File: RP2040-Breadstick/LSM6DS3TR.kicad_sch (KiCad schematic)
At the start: 1 part

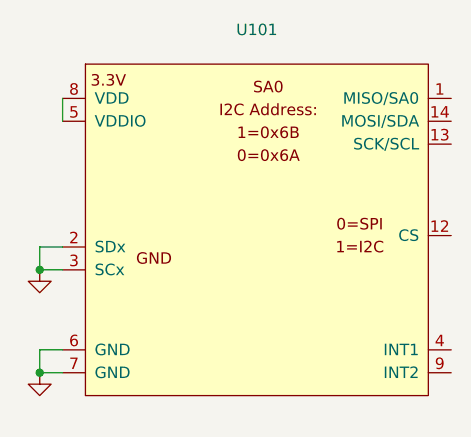
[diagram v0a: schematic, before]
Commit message: Moved Label R108
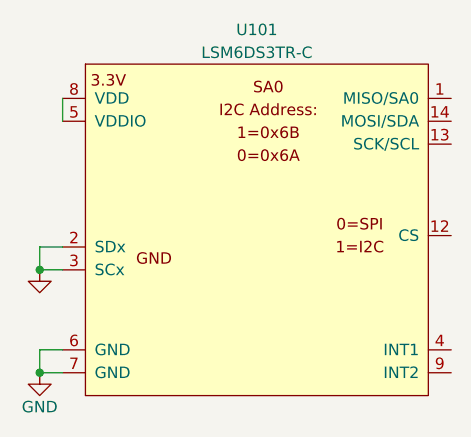
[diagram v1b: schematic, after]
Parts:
- U101: value (none) -> LSM6DS3TR-C; footprint (none) -> LSM6DS3TR-C:LGA-14-2.5X3MM
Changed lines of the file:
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@@
       (effects (font (size 1.27 1.27)) hide)
     )
-    (property "Value" "" (id 1) (at 115.57 102.87 0))
+    (property "Value" "GND" (id 1) (at 115.57 102.87 0))
     (property "Footprint" "" (id 2) (at 115.57 99.06 0)
       (effects (font (size 1.27 1.27)) hide)
@@
     (in_bom yes) (on_board yes) (fields_autoplaced)
     (property "Reference" "U101" (id 0) (at 139.7 60.96 0))
-    (property "Value" "" (id 1) (at 139.7 63.5 0))
-    (property "Footprint" "" (id 2) (at 125.73 104.14 0)
+    (property "Value" "LSM6DS3TR-C" (id 1) (at 139.7 63.5 0))
+    (property "Footprint" "LSM6DS3TR-C:LGA-14-2.5X3MM" (id 2) (at 125.73 104.14 0)
       (effects (font (size 1.27 1.27)) (justify left bottom) hide)
     )

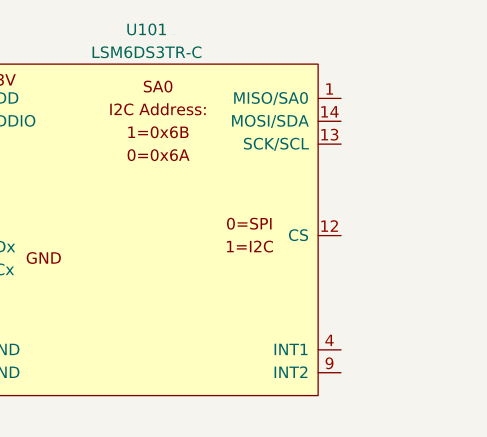
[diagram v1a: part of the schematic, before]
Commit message: IMU Pins and Power Supply updated
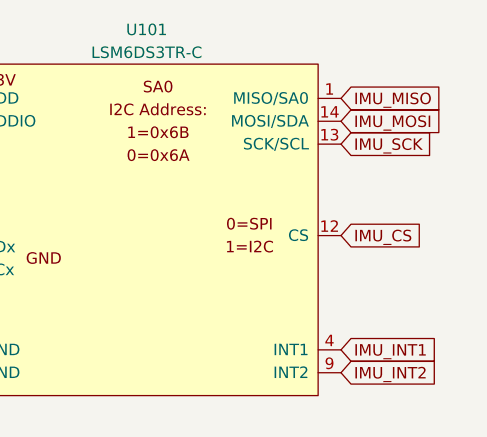
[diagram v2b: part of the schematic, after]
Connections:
- net IMU_MISO: now reaches U101.1 (MISO/SA0)
- net IMU_CS: now reaches U101.12 (CS)
- net IMU_SCK: now reaches U101.13 (SCK/SCL)
- net IMU_MOSI: now reaches U101.14 (MOSI/SDA)
- net IMU_INT1: now reaches U101.4 (INT1)
- net IMU_INT2: now reaches U101.9 (INT2)
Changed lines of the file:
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@@
     (stroke (width 0) (type default) (color 0 0 0 0))
+  )
+  (global_label "IMU_MISO" (shape input) (at 161.29 68.58 0) (fields_autoplaced)
+    (effects (font (size 1.27 1.27)) (justify left))
+    (property "Intersheet References" "${INTERSHEET_REFS}" (id 0) (at 172.6536 68.5006 0)
+      (effects (font (size 1.27 1.27)) (justify left) hide)
+    )
+  )
+  (global_label "IMU_INT1" (shape input) (at 161.29 96.52 0) (fields_autoplaced)
+    (effects (font (size 1.27 1.27)) (justify left))
+    (property "Intersheet References" "${INTERSHEET_REFS}" (id 0) (at 172.1698 96.4406 0)
+      (effects (font (size 1.27 1.27)) (justify left) hide)
+    )
+  )
+  (global_label "IMU_INT2" (shape input) (at 161.29 99.06 0) (fields_autoplaced)
+    (effects (font (size 1.27 1.27)) (justify left))
+    (property "Intersheet References" "${INTERSHEET_REFS}" (id 0) (at 172.1698 98.9806 0)
+      (effects (font (size 1.27 1.27)) (justify left) hide)
+    )
+  )
+  (global_label "IMU_CS" (shape input) (at 161.29 83.82 0) (fields_autoplaced)
+    (effects (font (size 1.27 1.27)) (justify left))
+    (property "Intersheet References" "${INTERSHEET_REFS}" (id 0) (at 170.5369 83.7406 0)
+      (effects (font (size 1.27 1.27)) (justify left) hide)
+    )
+  )
+  (global_label "IMU_SCK" (shape input) (at 161.29 73.66 0) (fields_autoplaced)
+    (effects (font (size 1.27 1.27)) (justify left))
+    (property "Intersheet References" "${INTERSHEET_REFS}" (id 0) (at 171.8069 73.5806 0)
+      (effects (font (size 1.27 1.27)) (justify left) hide)
+    )
+  )
+  (global_label "IMU_MOSI" (shape input) (at 161.29 71.12 0) (fields_autoplaced)
+    (effects (font (size 1.27 1.27)) (justify left))
+    (property "Intersheet References" "${INTERSHEET_REFS}" (id 0) (at 172.6536 71.0406 0)
+      (effects (font (size 1.27 1.27)) (justify left) hide)
+    )
   )
   (symbol (lib_id "power:GND") (at 115.57 99.06 0) (unit 1)

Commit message: Schematic Rough Draft Complete
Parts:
- added C401: 1uF, Breadstick Footprints:Perfect_0201_Cap, symbol Device:C
- renumbered U101 to U401
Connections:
- net GND: now also C401.2
- net 3V3_LDO: now reaches U401.5 (VDDIO), U401.8 (VDD)
- net 3V3_LDO: now also C401.1
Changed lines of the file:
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@@
   (junction (at 115.57 99.06) (diameter 0) (color 0 0 0 0)
+  )
+  (junction (at 118.11 68.58) (diameter 0) (color 0 0 0 0)
+  )
+  (junction (at 105.41 68.58) (diameter 0) (color 0 0 0 0)
   )
   (wire (pts (xy 115.57 85.09) (xy 115.57 87.63))
@@
     (stroke (width 0) (type default) (color 0 0 0 0))
   )
+  (wire (pts (xy 105.41 68.58) (xy 118.11 68.58))
+    (stroke (width 0) (type default) (color 0 0 0 0))
+  )
   (wire (pts (xy 115.57 96.52) (xy 115.57 99.06))
     (stroke (width 0) (type default) (color 0 0 0 0))
@@
   )
   (wire (pts (xy 118.11 85.09) (xy 115.57 85.09))
+    (stroke (width 0) (type default) (color 0 0 0 0))
+  )
+  (wire (pts (xy 105.41 66.04) (xy 105.41 68.58))
     (stroke (width 0) (type default) (color 0 0 0 0))
   )
@@
     )
   )
+  (global_label "3V3_LDO" (shape input) (at 105.41 66.04 180) (fields_autoplaced)
+    (effects (font (size 1.27 1.27)) (justify right))
+    (property "Intersheet References" "${INTERSHEET_REFS}" (id 0) (at 94.8931 66.1194 0)
+      (effects (font (size 1.27 1.27)) (justify right) hide)
+    )
+  )
   (global_label "IMU_MOSI" (shape input) (at 161.29 71.12 0) (fields_autoplaced)
     (effects (font (size 1.27 1.27)) (justify left))
@@
   (symbol (lib_id "power:GND") (at 115.57 99.06 0) (unit 1)
     (in_bom yes) (on_board yes)
-    (property "Reference" "#PWR0107" (id 0) (at 115.57 105.41 0)
+    (property "Reference" "#PWR0403" (id 0) (at 115.57 105.41 0)
       (effects (font (size 1.27 1.27)) hide)
     )
@@
   (symbol (lib_id "LSM6DS3TR-C:LSM6DS3TR-C") (at 139.7 83.82 0) (unit 1)
     (in_bom yes) (on_board yes) (fields_autoplaced)
-    (property "Reference" "U101" (id 0) (at 139.7 60.96 0))
+    (property "Reference" "U401" (id 0) (at 139.7 60.96 0))
     (property "Value" "LSM6DS3TR-C" (id 1) (at 139.7 63.5 0))
     (property "Footprint" "LSM6DS3TR-C:LGA-14-2.5X3MM" (id 2) (at 125.73 104.14 0)
@@
   (symbol (lib_id "power:GND") (at 115.57 87.63 0) (unit 1)
     (in_bom yes) (on_board yes)
-    (property "Reference" "#PWR0106" (id 0) (at 115.57 93.98 0)
+    (property "Reference" "#PWR0402" (id 0) (at 115.57 93.98 0)
       (effects (font (size 1.27 1.27)) hide)
     )
@@
     (pin "1")
   )
+  (symbol (lib_id "power:GND") (at 105.41 76.2 0) (unit 1)
+    (in_bom yes) (on_board yes)
+    (property "Reference" "#PWR0401" (id 0) (at 105.41 82.55 0)
+      (effects (font (size 1.27 1.27)) hide)
+    )
+    (property "Value" "~" (id 1) (at 105.41 80.01 0))
+    (property "Footprint" "" (id 2) (at 105.41 76.2 0)
+      (effects (font (size 1.27 1.27)) hide)
+    )
+    (property "Datasheet" "" (id 3) (at 105.41 76.2 0)
+      (effects (font (size 1.27 1.27)) hide)
+    )
+    (pin "1")
+  )
+  (symbol (lib_id "Device:C") (at 105.41 72.39 0) (unit 1)
+    (in_bom yes) (on_board yes) (fields_autoplaced)
+    (property "Reference" "C401" (id 0) (at 110.49 71.1199 0)
+      (effects (font (size 1.27 1.27)) (justify left))
+    )
+    (property "Value" "1uF" (id 1) (at 110.49 73.6599 0)
+      (effects (font (size 1.27 1.27)) (justify left))
+    )
+    (property "Footprint" "Breadstick Footprints:Perfect_0201_Cap" (id 2) (at 106.3752 76.2 0)
+      (effects (font (size 1.27 1.27)) hide)
+    )
+    (property "Datasheet" "~" (id 3) (at 105.41 72.39 0)
+      (effects (font (size 1.27 1.27)) hide)
+    )
+    (property "JLCPCB P/N" "C541330" (id 4) (at 105.41 72.39 0)
+      (effects (font (size 1.27 1.27)) hide)
+    )
+    (pin "1")
+    (pin "2")
+  )
 )

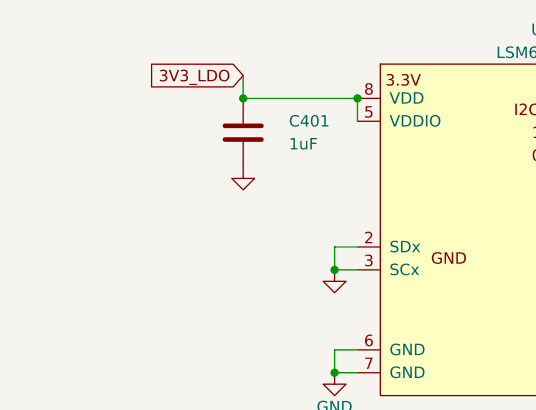
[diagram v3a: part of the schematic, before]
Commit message: Figuring Out IMU and Level Shifter Routing
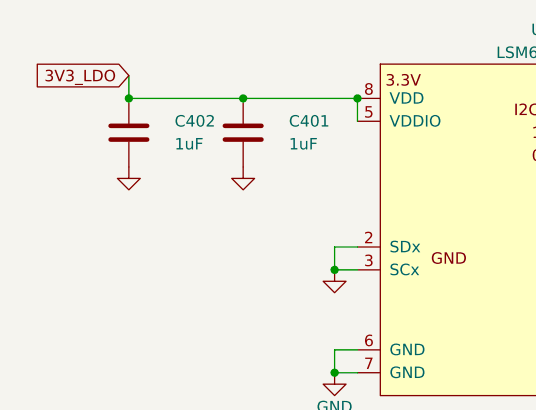
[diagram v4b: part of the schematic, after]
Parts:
- added C402: 1uF, Breadstick Footprints:Perfect_0201_Cap, symbol Device:C
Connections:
- net 3V3_LDO: now also C402.1
- net GND: now also C402.2
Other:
- company: (none) -> J & R Creative Technologies Inc.
- title: (none) -> RP2040 Breadstick
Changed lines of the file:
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@@
 (kicad_sch (version 20211123) (generator eeschema)
   (paper "A4")
+  (title_block
+    (title "RP2040 Breadstick")
+    (date "2022-08-10")
+    (rev "0.1")
+    (company "J & R Creative Technologies Inc.")
+    (comment 1 "@RangenMichael")
+    (comment 2 "https://twitter.com/RangenMichael")
+    (comment 3 "Apache-2.0 License")
+    (comment 4 "https://github.com/mrangen/RP2040-Breadstick")
+  )
+  (junction (at 92.71 68.58) (diameter 0) (color 0 0 0 0)
+  )
   (junction (at 115.57 87.63) (diameter 0) (color 0 0 0 0)
   )
   (junction (at 115.57 99.06) (diameter 0) (color 0 0 0 0)
   )
+  (junction (at 105.41 68.58) (diameter 0) (color 0 0 0 0)
+  )
   (junction (at 118.11 68.58) (diameter 0) (color 0 0 0 0)
   )
-  (junction (at 105.41 68.58) (diameter 0) (color 0 0 0 0)
-  )
   (wire (pts (xy 115.57 85.09) (xy 115.57 87.63))
     (stroke (width 0) (type default) (color 0 0 0 0))
   )
+  (wire (pts (xy 92.71 68.58) (xy 105.41 68.58))
+    (stroke (width 0) (type default) (color 0 0 0 0))
+  )
   (wire (pts (xy 115.57 87.63) (xy 118.11 87.63))
     (stroke (width 0) (type default) (color 0 0 0 0))
@@
     (stroke (width 0) (type default) (color 0 0 0 0))
   )
-  (wire (pts (xy 105.41 66.04) (xy 105.41 68.58))
+  (wire (pts (xy 92.71 66.04) (xy 92.71 68.58))
     (stroke (width 0) (type default) (color 0 0 0 0))
   )
@@
     )
   )
-  (global_label "3V3_LDO" (shape input) (at 105.41 66.04 180) (fields_autoplaced)
+  (global_label "3V3_LDO" (shape input) (at 92.71 66.04 180) (fields_autoplaced)
     (effects (font (size 1.27 1.27)) (justify right))
-    (property "Intersheet References" "${INTERSHEET_REFS}" (id 0) (at 94.8931 66.1194 0)
+    (property "Intersheet References" "${INTERSHEET_REFS}" (id 0) (at 82.1931 66.1194 0)
       (effects (font (size 1.27 1.27)) (justify right) hide)
     )
@@
       (effects (font (size 1.27 1.27)) hide)
     )
+    (pin "1")
+    (pin "2")
+  )
+  (symbol (lib_id "power:GND") (at 92.71 76.2 0) (unit 1)
+    (in_bom yes) (on_board yes)
+    (property "Reference" "#PWR0404" (id 0) (at 92.71 82.55 0)
+      (effects (font (size 1.27 1.27)) hide)
+    )
+    (property "Value" "~" (id 1) (at 92.71 80.01 0))
+    (property "Footprint" "" (id 2) (at 92.71 76.2 0)
+      (effects (font (size 1.27 1.27)) hide)
+    )
+    (property "Datasheet" "" (id 3) (at 92.71 76.2 0)
+      (effects (font (size 1.27 1.27)) hide)
+    )
+    (pin "1")
+  )
+  (symbol (lib_id "Device:C") (at 92.71 72.39 0) (unit 1)
+    (in_bom yes) (on_board yes) (fields_autoplaced)
+    (property "Reference" "C402" (id 0) (at 97.79 71.1199 0)
+      (effects (font (size 1.27 1.27)) (justify left))
+    )
+    (property "Value" "1uF" (id 1) (at 97.79 73.6599 0)
+      (effects (font (size 1.27 1.27)) (justify left))
+    )
+    (property "Footprint" "Breadstick Footprints:Perfect_0201_Cap" (id 2) (at 93.6752 76.2 0)
+      (effects (font (size 1.27 1.27)) hide)
+    )
+    (property "Datasheet" "~" (id 3) (at 92.71 72.39 0)
+      (effects (font (size 1.27 1.27)) hide)
+    )
+    (property "JLCPCB P/N" "C541330" (id 4) (at 92.71 72.39 0)
+      (effects (font (size 1.27 1.27)) hide)
+    )

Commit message: Added Digikey Part Numbers to BOM
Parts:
- C401, C402: footprint Breadstick Footprints:Perfect_0201_Cap -> (none)
- U401: footprint LSM6DS3TR-C:LGA-14-2.5X3MM -> (none)
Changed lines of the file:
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@@
     (property "Reference" "U401" (id 0) (at 139.7 60.96 0))
     (property "Value" "LSM6DS3TR-C" (id 1) (at 139.7 63.5 0))
-    (property "Footprint" "LSM6DS3TR-C:LGA-14-2.5X3MM" (id 2) (at 125.73 104.14 0)
+    (property "Footprint" "" (id 2) (at 125.73 104.14 0)
       (effects (font (size 1.27 1.27)) (justify left bottom) hide)
     )
@@
       (effects (font (size 1.27 1.27)) (justify left))
     )
-    (property "Footprint" "Breadstick Footprints:Perfect_0201_Cap" (id 2) (at 106.3752 76.2 0)
+    (property "Footprint" "" (id 2) (at 106.3752 76.2 0)
       (effects (font (size 1.27 1.27)) hide)
     )
@@
       (effects (font (size 1.27 1.27)) (justify left))
     )
-    (property "Footprint" "Breadstick Footprints:Perfect_0201_Cap" (id 2) (at 93.6752 76.2 0)
+    (property "Footprint" "" (id 2) (at 93.6752 76.2 0)
       (effects (font (size 1.27 1.27)) hide)
     )

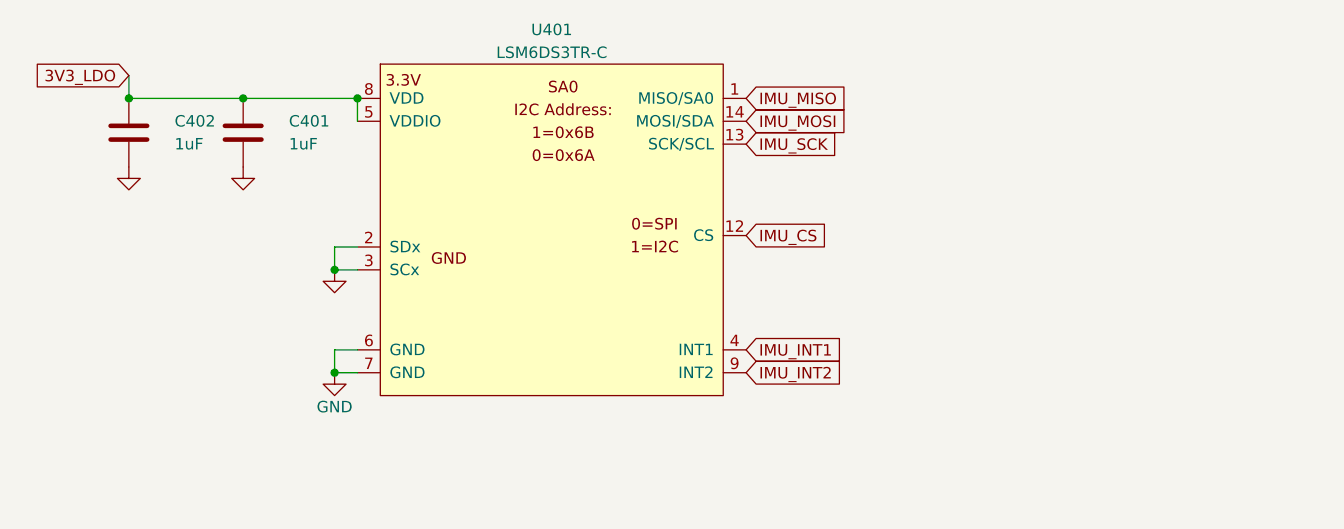
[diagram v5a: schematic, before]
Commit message: Initial Schematic Done, footprints roughly grouped on PCB
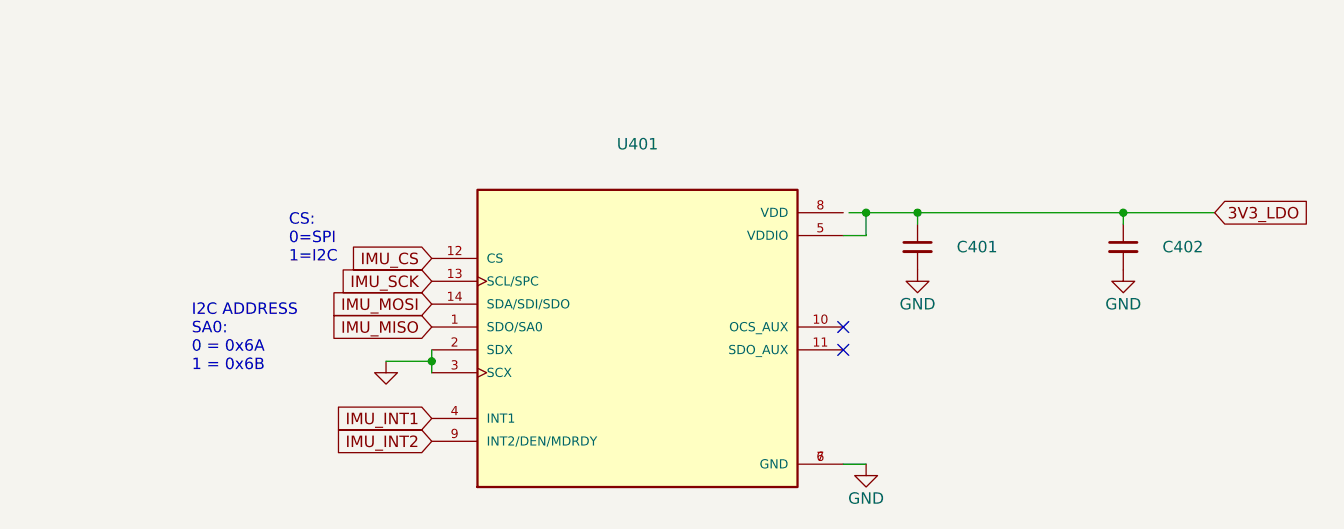
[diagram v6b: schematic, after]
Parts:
- removed C401, C402: 1uF, symbol Device:C
- removed U401: LSM6DS3TR-C, symbol LSM6DS3TR-C:LSM6DS3TR-C
- added C401, C402: (no value), symbol Device:C_Small
- added U401: (no value), symbol LSM6DSMTR:LSM6DSMTR
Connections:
- net 3V3_LDO: now also C401.1, C402.1, U401.5 (VDDIO)
- net GND: now also C401.2, C402.2, U401.2 (SDX), U401.3 (SCX), U401.6 (GND), U401.7 (GND)
- net IMU_CS: now also U401.12 (CS)
- net IMU_INT1: now also U401.4 (INT1)
- net IMU_INT2: now also U401.9 (INT2/DEN/MDRDY)
- net IMU_MISO: now also U401.1 (SDO/SA0)
- net IMU_MOSI: now also U401.14 (SDA/SDI/SDO)
- net IMU_SCK: now also U401.13 (SCL/SPC)
- no-connect marks 0 -> 2
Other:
- note added: "CS: 0=SPI 1=I2C"
- note added: "I2C ADDRESS SA0: 0 = 0x6A 1 = 0x6B"

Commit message: Worked on USB power section of PCB
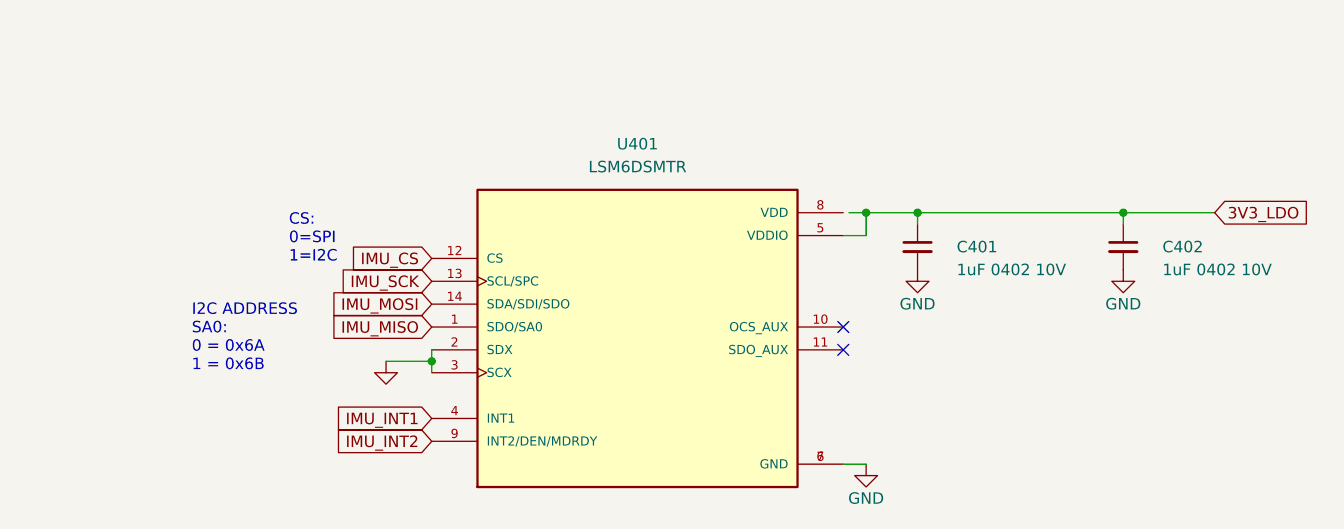
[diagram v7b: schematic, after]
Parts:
- C401, C402: value (none) -> 1uF 0402 10V; footprint (none) -> _Breadstick_Footprints:Perfect_0402_Cap
- U401: value (none) -> LSM6DSMTR; footprint (none) -> LSM6DSMTR:PQFN50P300X250X86-14N
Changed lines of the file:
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@@
       (effects (font (size 1.27 1.27)) (justify left))
     )
-    (property "Value" "" (id 1) (at 196.85 87.63 0)
+    (property "Value" "1uF 0402 10V" (id 1) (at 196.85 87.63 0)
       (effects (font (size 1.27 1.27)) (justify left))
     )
-    (property "Footprint" "" (id 2) (at 180.34 85.09 0)
+    (property "Footprint" "_Breadstick_Footprints:Perfect_0402_Cap" (id 2) (at 180.34 85.09 0)
       (effects (font (size 1.27 1.27)) hide)
     )
@@
       (effects (font (size 1.27 1.27)) (justify left))
     )
-    (property "Value" "" (id 1) (at 219.71 87.63 0)
+    (property "Value" "1uF 0402 10V" (id 1) (at 219.71 87.63 0)
       (effects (font (size 1.27 1.27)) (justify left))
     )
-    (property "Footprint" "" (id 2) (at 203.2 85.09 0)
+    (property "Footprint" "_Breadstick_Footprints:Perfect_0402_Cap" (id 2) (at 203.2 85.09 0)
       (effects (font (size 1.27 1.27)) hide)
     )
@@
     (in_bom yes) (on_board yes) (fields_autoplaced)
     (property "Reference" "U401" (id 0) (at 149.225 73.66 0))
-    (property "Value" "" (id 1) (at 149.225 76.2 0))
-    (property "Footprint" "" (id 2) (at 149.225 93.98 0)
+    (property "Value" "LSM6DSMTR" (id 1) (at 149.225 76.2 0))
+    (property "Footprint" "LSM6DSMTR:PQFN50P300X250X86-14N" (id 2) (at 149.225 93.98 0)
       (effects (font (size 1.27 1.27)) (justify bottom) hide)
     )
